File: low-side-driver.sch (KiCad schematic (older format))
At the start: 4 parts, among them U2 74HC595

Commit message: Add preliminary ESP32 power layout
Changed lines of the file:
@@
 $Descr A4 11693 8268
 encoding utf-8
-Sheet 8 25
+Sheet 18 25
 Title ""
 Date ""
@@
 AR Path="/61C4C905/61A75B6D/61A5FAFA" Ref="#PWR0153"  Part="1"
 AR Path="/61C4C905/61A75B93/61A5FAFA" Ref="#PWR0156"  Part="1"
-F 0 "#PWR0156" H 4900 3900 50  0001 C CNN
+F 0 "#PWR0141" H 4900 3900 50  0001 C CNN
 F 1 "GND" H 4905 3977 50  0000 C CNN
 F 2 "" H 4900 4150 50  0001 C CNN
@@
 AR Path="/61C4C905/61A75B6D/61A64A59" Ref="#PWR0154"  Part="1"
 AR Path="/61C4C905/61A75B93/61A64A59" Ref="#PWR0157"  Part="1"
-F 0 "#PWR0157" H 5350 2500 50  0001 C CNN
+F 0 "#PWR0142" H 5350 2500 50  0001 C CNN
 F 1 "GND" H 5355 2577 50  0000 C CNN
 F 2 "" H 5350 2750 50  0001 C CNN
@@
 AR Path="/61C4C905/61A75B6D/61A63F1A" Ref="C18"  Part="1"
 AR Path="/61C4C905/61A75B93/61A63F1A" Ref="C19"  Part="1"
-F 0 "C19" V 4921 2750 50  0000 C CNN
+F 0 "C14" V 4921 2750 50  0000 C CNN
 F 1 "100nF" V 5012 2750 50  0000 C CNN
 F 2 "Capacitor_SMD:C_0402_1005Metric" H 5150 2750 50  0001 C CNN
@@
 AR Path="/61C4C905/61A75B6D/61A5EC64" Ref="#PWR0155"  Part="1"
 AR Path="/61C4C905/61A75B93/61A5EC64" Ref="#PWR0158"  Part="1"
-F 0 "#PWR0158" H 4900 2550 50  0001 C CNN
+F 0 "#PWR0143" H 4900 2550 50  0001 C CNN
 F 1 "VBUS" H 4915 2873 50  0000 C CNN
 F 2 "" H 4900 2700 50  0001 C CNN
@@
 AR Path="/61C4C905/61A75B6D/61A5E6B7" Ref="RN34"  Part="1"
 AR Path="/61C4C905/61A75B93/61A5E6B7" Ref="RN36"  Part="1"
-F 0 "RN36" V 3833 3600 50  0000 C CNN
+F 0 "RN26" V 3833 3600 50  0000 C CNN
 F 1 "56R" V 3924 3600 50  0000 C CNN
 F 2 "Resistor_SMD:R_Array_Concave_4x0402" V 4525 3600 50  0001 C CNN
@@
 AR Path="/61C4C905/61A75B6D/61A5E6AC" Ref="RN33"  Part="1"
 AR Path="/61C4C905/61A75B93/61A5E6AC" Ref="RN35"  Part="1"
-F 0 "RN35" V 3833 3200 50  0000 C CNN
+F 0 "RN25" V 3833 3200 50  0000 C CNN
 F 1 "56R" V 3924 3200 50  0000 C CNN
 F 2 "Resistor_SMD:R_Array_Concave_4x0402" V 4525 3200 50  0001 C CNN
@@
 AR Path="/61C4C905/61A75B6D/61A5E6A5" Ref="U21"  Part="1"
 AR Path="/61C4C905/61A75B93/61A5E6A5" Ref="U22"  Part="1"
-F 0 "U22" H 5100 3950 50  0000 C CNN
+F 0 "U17" H 5100 3950 50  0000 C CNN
 F 1 "74HC595" V 4950 3350 50  0000 C CNN
 F 2 "Package_Texas:X1QFN-16-2.5x2.5-EP-1.2" H 4900 3400 50  0001 C CNN

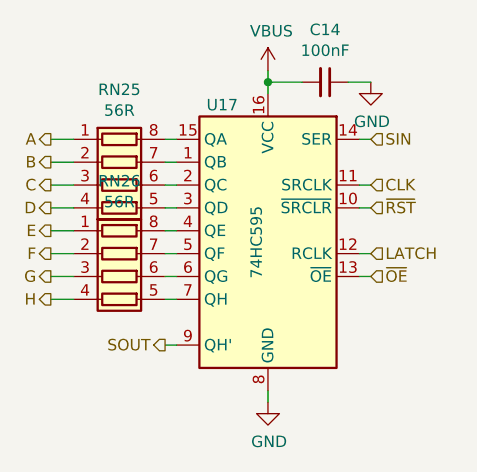
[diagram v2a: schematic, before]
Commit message: Layout horizontal busses
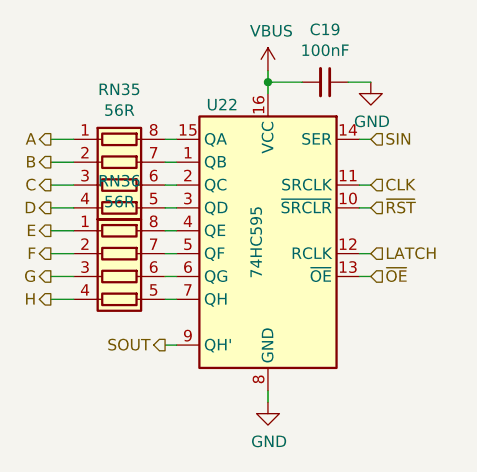
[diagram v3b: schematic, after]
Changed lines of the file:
@@
 $Descr A4 11693 8268
 encoding utf-8
-Sheet 18 25
+Sheet 23 25
 Title ""
 Date ""
@@
 AR Path="/61C4C905/61A75B6D/61A5FAFA" Ref="#PWR0153"  Part="1"
 AR Path="/61C4C905/61A75B93/61A5FAFA" Ref="#PWR0156"  Part="1"
-F 0 "#PWR0141" H 4900 3900 50  0001 C CNN
+F 0 "#PWR0156" H 4900 3900 50  0001 C CNN
 F 1 "GND" H 4905 3977 50  0000 C CNN
 F 2 "" H 4900 4150 50  0001 C CNN
@@
 AR Path="/61C4C905/61A75B6D/61A64A59" Ref="#PWR0154"  Part="1"
 AR Path="/61C4C905/61A75B93/61A64A59" Ref="#PWR0157"  Part="1"
-F 0 "#PWR0142" H 5350 2500 50  0001 C CNN
+F 0 "#PWR0157" H 5350 2500 50  0001 C CNN
 F 1 "GND" H 5355 2577 50  0000 C CNN
 F 2 "" H 5350 2750 50  0001 C CNN
@@
 AR Path="/61C4C905/61A75B6D/61A63F1A" Ref="C18"  Part="1"
 AR Path="/61C4C905/61A75B93/61A63F1A" Ref="C19"  Part="1"
-F 0 "C14" V 4921 2750 50  0000 C CNN
+F 0 "C19" V 4921 2750 50  0000 C CNN
 F 1 "100nF" V 5012 2750 50  0000 C CNN
 F 2 "Capacitor_SMD:C_0402_1005Metric" H 5150 2750 50  0001 C CNN
@@
 AR Path="/61C4C905/61A75B6D/61A5EC64" Ref="#PWR0155"  Part="1"
 AR Path="/61C4C905/61A75B93/61A5EC64" Ref="#PWR0158"  Part="1"
-F 0 "#PWR0143" H 4900 2550 50  0001 C CNN
+F 0 "#PWR0158" H 4900 2550 50  0001 C CNN
 F 1 "VBUS" H 4915 2873 50  0000 C CNN
 F 2 "" H 4900 2700 50  0001 C CNN
@@
 AR Path="/61C4C905/61A75B6D/61A5E6B7" Ref="RN34"  Part="1"
 AR Path="/61C4C905/61A75B93/61A5E6B7" Ref="RN36"  Part="1"
-F 0 "RN26" V 3833 3600 50  0000 C CNN
+F 0 "RN36" V 3833 3600 50  0000 C CNN
 F 1 "56R" V 3924 3600 50  0000 C CNN
 F 2 "Resistor_SMD:R_Array_Concave_4x0402" V 4525 3600 50  0001 C CNN
@@
 AR Path="/61C4C905/61A75B6D/61A5E6AC" Ref="RN33"  Part="1"
 AR Path="/61C4C905/61A75B93/61A5E6AC" Ref="RN35"  Part="1"
-F 0 "RN25" V 3833 3200 50  0000 C CNN
+F 0 "RN35" V 3833 3200 50  0000 C CNN
 F 1 "56R" V 3924 3200 50  0000 C CNN
 F 2 "Resistor_SMD:R_Array_Concave_4x0402" V 4525 3200 50  0001 C CNN
@@
 AR Path="/61C4C905/61A75B6D/61A5E6A5" Ref="U21"  Part="1"
 AR Path="/61C4C905/61A75B93/61A5E6A5" Ref="U22"  Part="1"
-F 0 "U17" H 5100 3950 50  0000 C CNN
+F 0 "U22" H 5100 3950 50  0000 C CNN
 F 1 "74HC595" V 4950 3350 50  0000 C CNN
 F 2 "Package_Texas:X1QFN-16-2.5x2.5-EP-1.2" H 4900 3400 50  0001 C CNN
